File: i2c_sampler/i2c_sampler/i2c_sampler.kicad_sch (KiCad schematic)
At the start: 55 parts, among them J1 Conn_01x04, J10 Conn_01x03, J11 Conn_01x03, J12 Barrel_Jack_Switch, J13 Conn_01x04, J2 Conn_01x03, J3 Conn_01x03, J4 Conn_01x03, J5 Conn_01x03, J6 Conn_01x03, J7 Conn_01x03, J8 Conn_02x10_Odd_Even, J9 Conn_01x03, Q1 Q_PMOS_GSD, U1 DS2482-100, U2 DS1307Z+, U3 TPS613222ADBV, U4 MCP1640BCH, U5 LM75B, U6 MCP23017_SO, U7 AP62200, Y1 Crystal

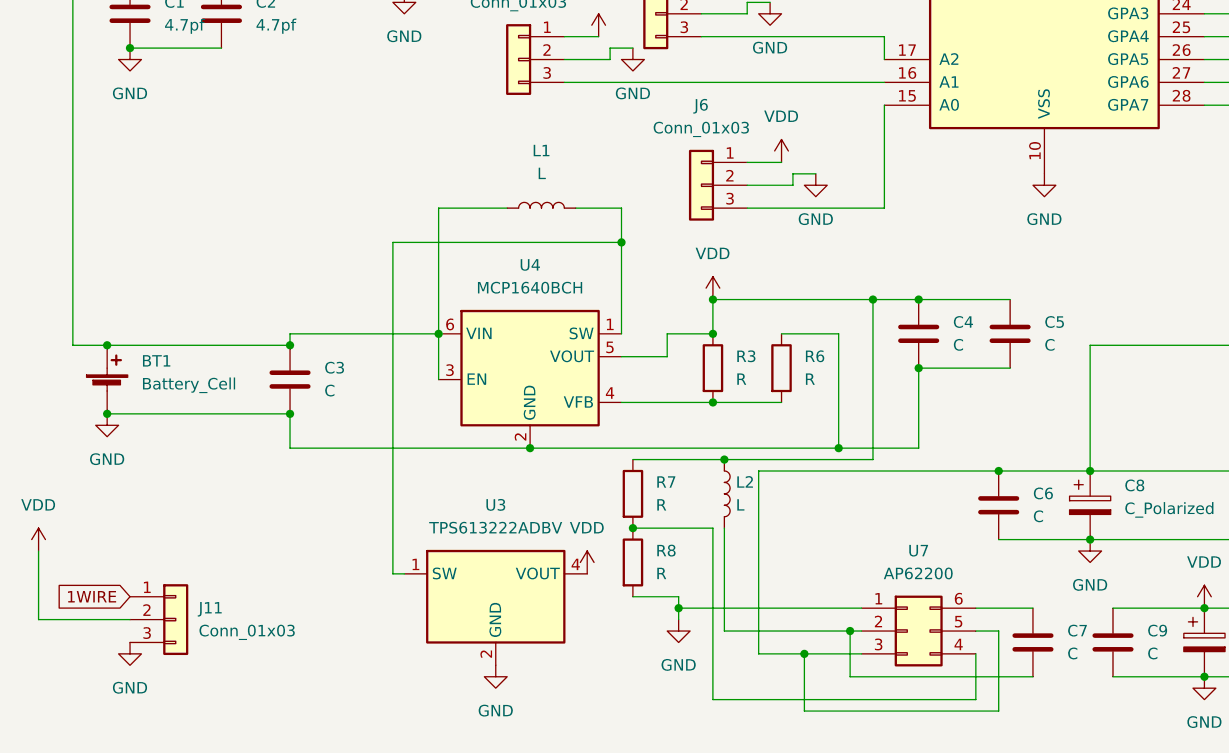
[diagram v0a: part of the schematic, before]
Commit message: Update I2C sampler and IoTether, add voltage converter
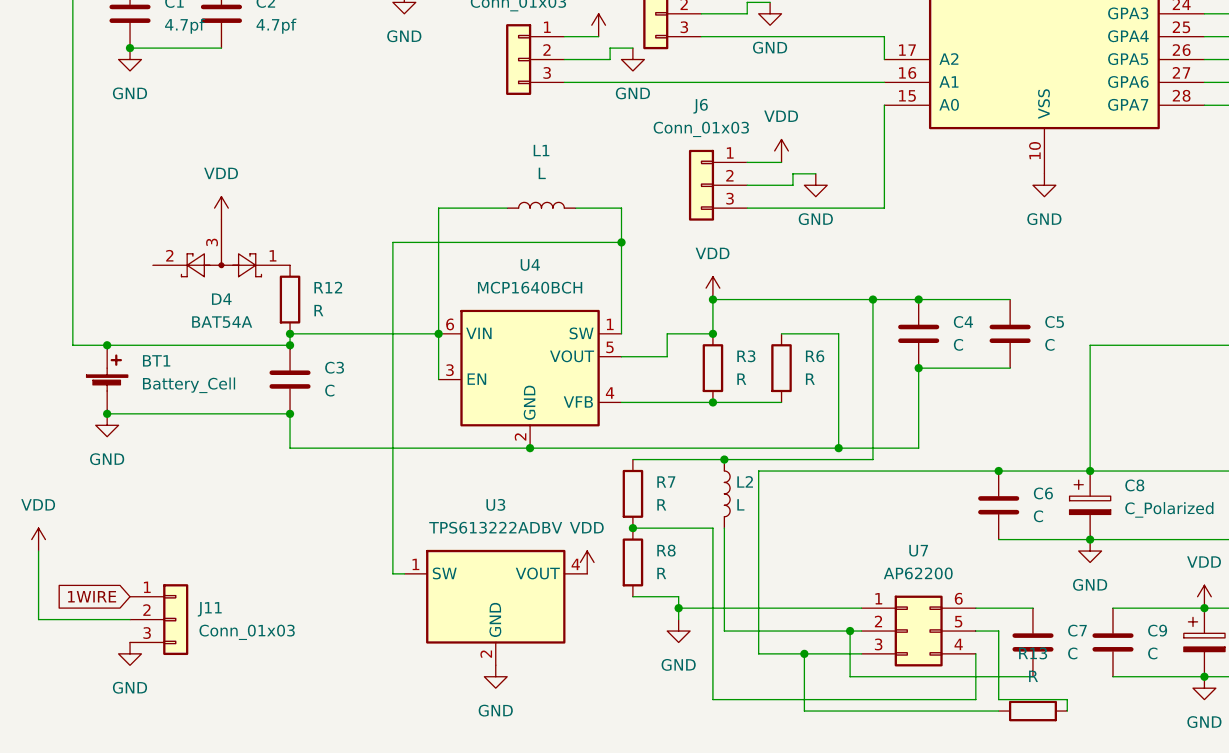
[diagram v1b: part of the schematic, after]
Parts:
- added D4: BAT54A, Package_TO_SOT_SMD:SOT-23, symbol Diode:BAT54A
- added R12, R13: R, Resistor_SMD:R_0603_1608Metric, symbol Device:R
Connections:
- net VDD: now also D4.3
- net at BT1.1 (+), C3.1, L1.1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: now also R12.2
- net at C11.1, C6.1, C8.1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: now also R13.1; no longer U7.5 (Pin_5)
- new net: R13.2, U7.5 (Pin_5)
- new net: D4.1, R12.1
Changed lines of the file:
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@@
   (junction (at 148.59 58.42) (diameter 0) (color 0 0 0 0)
   )
+  (junction (at 43.18 153.67) (diameter 0) (color 0 0 0 0)
+  )
   (junction (at 118.11 25.4) (diameter 0) (color 0 0 0 0)
   )
@@
     (stroke (width 0) (type default) (color 0 0 0 0))
   )
+  (wire (pts (xy 129.54 194.31) (xy 129.54 195.58))
+    (stroke (width 0) (type default) (color 0 0 0 0))
+  )
   (wire (pts (xy 46.99 52.07) (xy 85.09 52.07))
     (stroke (width 0) (type default) (color 0 0 0 0))
@@
     (stroke (width 0) (type default) (color 0 0 0 0))
   )
-  (wire (pts (xy 121.92 186.69) (xy 121.92 195.58))
-    (stroke (width 0) (type default) (color 0 0 0 0))
-  )
   (wire (pts (xy 35.56 107.95) (xy 35.56 114.3))
     (stroke (width 0) (type default) (color 0 0 0 0))
@@
     (stroke (width 0) (type default) (color 0 0 0 0))
   )
+  (wire (pts (xy 121.92 186.69) (xy 121.92 194.31))
+    (stroke (width 0) (type default) (color 0 0 0 0))
+  )
   (wire (pts (xy 52.07 69.85) (xy 52.07 76.2))
     (stroke (width 0) (type default) (color 0 0 0 0))
@@
   )
   (wire (pts (xy 95.25 189.23) (xy 95.25 168.91))
+    (stroke (width 0) (type default) (color 0 0 0 0))
+  )
+  (wire (pts (xy 121.92 194.31) (xy 129.54 194.31))
     (stroke (width 0) (type default) (color 0 0 0 0))
   )
@@
     )
     (pin "1")
+  )
+  (symbol (lib_id "Device:R") (at 125.73 195.58 90) (unit 1)
+    (in_bom yes) (on_board yes) (fields_autoplaced)
+    (property "Reference" "R13" (id 0) (at 125.73 189.23 90))
+    (property "Value" "R" (id 1) (at 125.73 191.77 90))
+    (property "Footprint" "Resistor_SMD:R_0603_1608Metric" (id 2) (at 125.73 197.358 90)
+      (effects (font (size 1.27 1.27)) hide)
+    )
+    (property "Datasheet" "~" (id 3) (at 125.73 195.58 0)
+      (effects (font (size 1.27 1.27)) hide)
+    )
+    (pin "1")
+    (pin "2")
   )
   (symbol (lib_id "Connector:Barrel_Jack_Switch") (at 160.02 157.48 0) (mirror y) (unit 1)
@@
     (pin "1")
   )
+  (symbol (lib_id "Device:R") (at 43.18 149.86 0) (unit 1)
+    (in_bom yes) (on_board yes) (fields_autoplaced)
+    (property "Reference" "R12" (id 0) (at 45.72 148.5899 0)
+      (effects (font (size 1.27 1.27)) (justify left))
+    )
+    (property "Value" "R" (id 1) (at 45.72 151.1299 0)
+      (effects (font (size 1.27 1.27)) (justify left))
+    )
+    (property "Footprint" "Resistor_SMD:R_0603_1608Metric" (id 2) (at 41.402 149.86 90)
+      (effects (font (size 1.27 1.27)) hide)
+    )
+    (property "Datasheet" "~" (id 3) (at 43.18 149.86 0)
+      (effects (font (size 1.27 1.27)) hide)
+    )
+    (pin "1")
+    (pin "2")
+  )
   (symbol (lib_id "Connector_Generic:Conn_01x03") (at 163.83 27.94 0) (unit 1)
     (in_bom yes) (on_board yes) (fields_autoplaced)
@@
     (pin "1")
   )
+  (symbol (lib_id "power:VDD") (at 35.56 140.97 0) (unit 1)
+    (in_bom yes) (on_board yes) (fields_autoplaced)
+    (property "Reference" "#PWR036" (id 0) (at 35.56 144.78 0)
+      (effects (font (size 1.27 1.27)) hide)
+    )
+    (property "Value" "VDD" (id 1) (at 35.56 135.89 0))
+    (property "Footprint" "" (id 2) (at 35.56 140.97 0)
+      (effects (font (size 1.27 1.27)) hide)
+    )
+    (property "Datasheet" "" (id 3) (at 35.56 140.97 0)
+      (effects (font (size 1.27 1.27)) hide)
+    )
+    (pin "1")
+  )
   (symbol (lib_id "Timer_RTC:DS1307Z+") (at 55.88 105.41 0) (unit 1)
     (in_bom yes) (on_board yes) (fields_autoplaced)
@@
     )
   )
+  (symbol (lib_id "Diode:BAT54A") (at 35.56 146.05 180) (unit 1)
+    (in_bom yes) (on_board yes) (fields_autoplaced)
+    (property "Reference" "D4" (id 0) (at 35.56 149.86 0))
+    (property "Value" "BAT54A" (id 1) (at 35.56 152.4 0))
+    (property "Footprint" "Package_TO_SOT_SMD:SOT-23" (id 2) (at 33.655 149.225 0)
+      (effects (font (size 1.27 1.27)) (justify left) hide)
+    )
+    (property "Datasheet" "http://www.diodes.com/_files/datasheets/ds11005.pdf" (id 3) (at 38.608 146.05 0)
+      (effects (font (size 1.27 1.27)) hide)
+    )
+    (pin "1")
+    (pin "2")
+    (pin "3")
+  )
   (symbol (lib_id "Device:C") (at 43.18 158.75 0) (unit 1)
     (in_bom yes) (on_board yes) (fields_autoplaced)
@@
       (reference "#PWR035") (unit 1) (value "GND") (footprint "")
     )
+    (path "/b111fe6c-384a-4659-a471-f0ccefc9f9e1"
+      (reference "#PWR036") (unit 1) (value "VDD") (footprint "")
+    )
     (path "/a4745e90-47d2-47b7-ba08-94a241d3fc97"
       (reference "BT1") (unit 1) (value "Battery_Cell") (footprint "Connector_PinHeader_2.54mm:PinHeader_1x02_P2.54mm_Vertical")
@@
       (reference "D3") (unit 1) (value "LED") (footprint "LED_THT:LED_D5.0mm")
     )
+    (path "/dc6cbb07-f89b-42a1-8bf4-0fc65a321d5b"
+      (reference "D4") (unit 1) (value "BAT54A") (footprint "Package_TO_SOT_SMD:SOT-23")
+    )
     (path "/f4f7122d-f244-4824-9ff0-3cd3b0363a23"
       (reference "H1") (unit 1) (value "MountingHole") (footprint "MountingHole:MountingHole_3.2mm_M3")
@@
       (reference "R11") (unit 1) (value "R") (footprint "Resistor_SMD:R_0603_1608Metric")
     )
+    (path "/7832d7a0-a237-4504-9f2e-4b7cdb437235"
+      (reference "R12") (unit 1) (value "R") (footprint "Resistor_SMD:R_0603_1608Metric")
+    )
+    (path "/1ce3a8dd-e182-4a77-9a6d-27881047d2e8"
+      (reference "R13") (unit 1) (value "R") (footprint "Resistor_SMD:R_0603_1608Metric")
+    )
     (path "/98000ede-242e-474b-94dc-db269970ebe0"

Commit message: Update IoTether and I2C sampler
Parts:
- added C13, C14, C15, C16: C, Capacitor_SMD:C_0805_2012Metric, symbol Device:C
- added D5, D6: LED, LED_SMD:LED_0603_1608Metric, symbol Device:LED
- added J14: Conn_01x09, Connector_USB:USB_A_Wuerth_61400826021_Horizontal_Stacked, symbol Connector_Generic:Conn_01x09
- added J15, J16: Conn_01x05, Library:009155003541006, symbol Connector_Generic:Conn_01x05
- added R14, R15, R16, R17: R, Resistor_SMD:R_0603_1608Metric, symbol Device:R
- added U8, U9: MCP73831-2-OT, Package_TO_SOT_SMD:SOT-23-5, symbol Battery_Management:MCP73831-2-OT
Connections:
- net GND: now also C13.2, C14.2, C15.2, C16.2, J14.4 (Pin_4), J14.8 (Pin_8), J14.9 (Pin_9), J15.3 (Pin_3), J15.4 (Pin_4), J15.5 (Pin_5), J16.3 (Pin_3), J16.4 (Pin_4), J16.5 (Pin_5), R14.2, R15.2, U8.2 (VSS), U9.2 (VSS)
- net VDD: now also C13.1, C14.1, J14.1 (Pin_1), J14.5 (Pin_5), R16.2, R17.2, U8.4 (VDD), U9.4 (VDD)
- new net: D5.1 (K), U8.1 (STAT)
- new net: C15.1, J15.1 (Pin_1), U8.3 (VBAT)
- new net: R14.1, U8.5 (PROG)
- new net: D5.2 (A), R16.1
- new net: J14.2 (Pin_2), J14.3 (Pin_3)
- new net: J14.6 (Pin_6), J14.7 (Pin_7)
- new net: D6.2 (A), R17.1
- new net: C16.1, J16.1 (Pin_1), U9.3 (VBAT)
- new net: R15.1, U9.5 (PROG)
- new net: D6.1 (K), U9.1 (STAT)
